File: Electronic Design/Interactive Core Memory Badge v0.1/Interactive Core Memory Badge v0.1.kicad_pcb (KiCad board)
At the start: 2 copper layers, 8 parts, among them Q1 MMBT4403LT1G, Q2 MMBT4401LT1G, U1 Teensy-LC

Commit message: Schematic Complete
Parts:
- removed the D1 at (103.5, 89.5)
- removed the D2 at (97.8, 86.4)
- removed the Q1 at (109.2, 95.2)
- removed the Q2 at (97.8, 95.2)
- removed the R1 at (104.5, 94.0)
- removed the R2 at (93.0, 94.0)
- added D1: BAW56S, Package_TO_SOT_SMD:SOT-363_SC-70-6, F.Cu at (99.1, 111.8)
- added D1: BAW56S, Package_TO_SOT_SMD:SOT-363_SC-70-6, F.Cu at (76.2, 111.8)
- added D2: BAV70S, Package_TO_SOT_SMD:SOT-363_SC-70-6, F.Cu at (99.1, 115.6)
- added D2: BAV70S, Package_TO_SOT_SMD:SOT-363_SC-70-6, F.Cu at (76.2, 115.6)
- added D3: BAW56S, Package_TO_SOT_SMD:SOT-363_SC-70-6, F.Cu at (110.2, 132.6)
- added D4: BAV70S, Package_TO_SOT_SMD:SOT-363_SC-70-6, F.Cu at (101.4, 140.5)
- added D5: BAW56S, Package_TO_SOT_SMD:SOT-363_SC-70-6, F.Cu at (63.0, 150.0)
- added D6: BAV70S, Package_TO_SOT_SMD:SOT-363_SC-70-6, F.Cu at (67.7, 147.0)
- added F1: Polyfuse, Fuse:Fuse_0805_2012Metric, F.Cu at (57.6, 160.7)
- added Q1: MMBT4403LT1G, Digikey:SOT-23-3, F.Cu at (89.9, 112.3)
- added Q1: MMBT4403LT1G, Digikey:SOT-23-3, F.Cu at (67.0, 112.3)
- added Q10: MMBT4401LT1G, Digikey:SOT-23-3, F.Cu at (45.0, 146.6)
- added Q11: MMBT4403LT1G, Digikey:SOT-23-3, F.Cu at (49.7, 141.7)
- added Q12: MMBT4401LT1G, Digikey:SOT-23-3, F.Cu at (45.0, 151.6)
- added Q13: MMBT4403LT1G, Digikey:SOT-23-3, F.Cu at (92.5, 135.2)
- added Q14: MMBT4401LT1G, Digikey:SOT-23-3, F.Cu at (87.8, 140.1)
- added Q15: MMBT4403LT1G, Digikey:SOT-23-3, F.Cu at (97.2, 130.2)
- added Q16: MMBT4401LT1G, Digikey:SOT-23-3, F.Cu at (92.5, 140.1)
- added Q17: MMBT4403LT1G, Digikey:SOT-23-3, F.Cu at (54.4, 141.7)
- added Q18: MMBT4401LT1G, Digikey:SOT-23-3, F.Cu at (49.7, 146.6)
- added Q19: MMBT4403LT1G, Digikey:SOT-23-3, F.Cu at (54.4, 146.6)
- added Q2: MMBT4401LT1G, Digikey:SOT-23-3, F.Cu at (94.6, 112.3)
- added Q2: MMBT4401LT1G, Digikey:SOT-23-3, F.Cu at (71.7, 112.3)
- added Q20: MMBT4401LT1G, Digikey:SOT-23-3, F.Cu at (49.7, 151.6)
- added Q21: MMBT4401LT1G, Digikey:SOT-23-3, F.Cu at (63.5, 188.0)
- added Q3: MMBT4403LT1G, Digikey:SOT-23-3, F.Cu at (83.1, 130.2)
- added Q4: MMBT4401LT1G, Digikey:SOT-23-3, F.Cu at (83.1, 135.2)
- added Q5: MMBT4403LT1G, Digikey:SOT-23-3, F.Cu at (87.8, 130.2)
- added Q6: MMBT4401LT1G, Digikey:SOT-23-3, F.Cu at (83.1, 140.1)
- added Q7: MMBT4403LT1G, Digikey:SOT-23-3, F.Cu at (92.5, 130.2)
- added Q8: MMBT4401LT1G, Digikey:SOT-23-3, F.Cu at (87.8, 135.2)
- added Q9: MMBT4403LT1G, Digikey:SOT-23-3, F.Cu at (45.0, 141.7)
- added R1: 220, Resistor_SMD:R_0805_2012Metric, F.Cu at (89.7, 116.3)
- added R1: 220, Resistor_SMD:R_0805_2012Metric, F.Cu at (66.9, 116.3)
- added R10: 6R8, Resistor_SMD:R_0805_2012Metric, F.Cu at (101.5, 134.2)
- added R11: 6R8, Resistor_SMD:R_0805_2012Metric, F.Cu at (59.0, 140.7)
- added R12: 6R8, Resistor_SMD:R_0805_2012Metric, F.Cu at (54.3, 150.6)
- added R13: 220, Resistor_SMD:R_0805_2012Metric, F.Cu at (101.5, 137.1)
- added R14: 220, Resistor_SMD:R_0805_2012Metric, F.Cu at (97.1, 140.1)
- added R15: 6R8, Resistor_SMD:R_0805_2012Metric, F.Cu at (105.9, 132.2)
- added R16: 220, Resistor_SMD:R_0805_2012Metric, F.Cu at (63.4, 140.7)
- added R17: 220, Resistor_SMD:R_0805_2012Metric, F.Cu at (59.0, 143.6)
- added R18: 220, Resistor_SMD:R_0805_2012Metric, F.Cu at (63.4, 143.6)
- added R19: 220, Resistor_SMD:R_0805_2012Metric, F.Cu at (59.0, 146.6)
- added R2: 220, Resistor_SMD:R_0805_2012Metric, F.Cu at (94.2, 116.3)
- added R2: 220, Resistor_SMD:R_0805_2012Metric, F.Cu at (71.3, 116.3)
- added R20: 220, Resistor_SMD:R_0805_2012Metric, F.Cu at (110.6, 129.2)
- added R21: 220, Resistor_SMD:R_0805_2012Metric, F.Cu at (105.9, 135.1)
- added R22: 6R8, Resistor_SMD:R_0805_2012Metric, F.Cu at (96.2, 144.1)
- added R23: 220, Resistor_SMD:R_0805_2012Metric, F.Cu at (58.7, 150.6)
- added R24: 220, Resistor_SMD:R_0805_2012Metric, F.Cu at (67.8, 140.7)
- added R25: 220, Resistor_SMD:R_0805_2012Metric, F.Cu at (63.4, 146.6)
- added R26: 220, Resistor_SMD:R_0805_2012Metric, F.Cu at (67.8, 143.6)
- added R27: 220, Resistor_SMD:R_0805_2012Metric, F.Cu at (68.1, 187.0)
- added R28: 1K5, Resistor_SMD:R_0805_2012Metric, F.Cu at (48.6, 82.5)
- added R29: 1K8, Resistor_SMD:R_0805_2012Metric, F.Cu at (67.7, 129.9)
- added R3: 220, Resistor_SMD:R_0805_2012Metric, F.Cu at (87.4, 144.1)
- added R30: 22, Resistor_SMD:R_0805_2012Metric, F.Cu at (67.7, 132.8)
- added R31: 1K5, Resistor_SMD:R_0805_2012Metric, F.Cu at (72.1, 129.9)
- added R32: 1K8, Resistor_SMD:R_0805_2012Metric, F.Cu at (67.7, 135.8)
- added R33: 22, Resistor_SMD:R_0805_2012Metric, F.Cu at (72.1, 132.8)
- added R34: 1K5, Resistor_SMD:R_0805_2012Metric, F.Cu at (76.5, 129.9)
- added R35: 10k, Resistor_SMD:R_0805_2012Metric, F.Cu at (72.1, 135.8)
- added R36: 10k, Resistor_SMD:R_0805_2012Metric, F.Cu at (62.7, 165.1)
- added R37: 10k, Resistor_SMD:R_0805_2012Metric, F.Cu at (62.6, 171.0)
- added R38: 4K7, Resistor_SMD:R_0805_2012Metric, F.Cu at (67.0, 171.3)
- added R39: 4K7, Resistor_SMD:R_0805_2012Metric, F.Cu at (67.0, 175.7)
- added R4: 220, Resistor_SMD:R_0805_2012Metric, F.Cu at (91.8, 144.1)
- added R5: 6R8, Resistor_SMD:R_0805_2012Metric, F.Cu at (83.0, 144.1)
- added R6: 220, Resistor_SMD:R_0805_2012Metric, F.Cu at (101.8, 129.2)
- added R7: 220, Resistor_SMD:R_0805_2012Metric, F.Cu at (97.1, 134.2)
- added R8: 220, Resistor_SMD:R_0805_2012Metric, F.Cu at (97.1, 137.1)
- added R9: 220, Resistor_SMD:R_0805_2012Metric, F.Cu at (106.2, 129.2)
- added SW1: SW_SPST, Digikey:Switch_Slide_JS202011SCQN, F.Cu at (48.3, 162.8)
- added U1: Micro_LiPo_Charger, Core_Memory_8x8_Array:Micro_LiPo_Charger, F.Cu at (54.6, 182.9)
- added U3: LM393, Digikey:SOIC-8_W3.9mm, F.Cu at (46.4, 91.3)
- moved CM1 43.3 mm to (83.8, 76.2)
- moved U2 41.5 mm to (83.8, 175.3)
- renumbered U1 to U2
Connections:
- net Net-(U1-Pad19) renamed AVAILABLE
- net Net-(U1-Pad37) renamed REED_SWITCH
- CM1 pad 1: XT0 -> XT0-4
- CM1 pad 10: Net-(CM1-Pad10) -> YL1
- CM1 pad 11: Net-(CM1-Pad11) -> YL2
- CM1 pad 12: Net-(CM1-Pad12) -> YL3
- CM1 pad 13: Net-(CM1-Pad13) -> YL4
- CM1 pad 14: Net-(CM1-Pad10) -> YL5
- CM1 pad 15: Net-(CM1-Pad11) -> YL4
- CM1 pad 16: Net-(CM1-Pad12) -> YL5
- CM1 pad 2: XT1 -> XT1-5
- CM1 pad 29: Net-(CM1-Pad29) -> Net-(CM1-Pad25)
- CM1 pad 3: XT2 -> XT2-6
- CM1 pad 30: Net-(CM1-Pad30) -> Net-(CM1-Pad26)
- CM1 pad 31: Net-(CM1-Pad31) -> Net-(CM1-Pad27)
- CM1 pad 32: Net-(CM1-Pad32) -> Net-(CM1-Pad28)
- CM1 pad 4: XT3 -> XT3-7
- CM1 pad 5: XT4 -> XT0-4
- CM1 pad 6: XT5 -> XT1-5
- CM1 pad 7: XT6 -> XT2-6
- CM1 pad 8: XT7 -> XT3-7
- CM1 pad 9: Net-(CM1-Pad13) -> YL0
- U2 pad 1: Net-(U1-Pad1) -> -BATT
- U2 pad 10: Net-(U1-Pad10) -> Q4N
- U2 pad 11: Net-(U1-Pad11) -> Q5P
- U2 pad 12: Net-(U1-Pad12) -> Q5N
- U2 pad 13: Net-(U1-Pad13) -> Q6P
- U2 pad 14: Net-(U1-Pad14) -> Q6N
- U2 pad 2: Net-(U1-Pad2) -> SENSE_PULSE
- U2 pad 20: Net-(U1-Pad20) -> Q7P
- U2 pad 21: Net-(U1-Pad21) -> Q7N
- U2 pad 22: Net-(U1-Pad22) -> Q8P
- U2 pad 23: Net-(U1-Pad23) -> Q8N
- U2 pad 24: Net-(U1-Pad24) -> Q9P
- U2 pad 25: Net-(U1-Pad25) -> I2C_DATA
- U2 pad 26: Net-(U1-Pad26) -> I2C_CLOCK
- U2 pad 27: Net-(U1-Pad27) -> Q9N
- U2 pad 28: Net-(U1-Pad28) -> Q10P
- U2 pad 29: Net-(U1-Pad29) -> Q10N
- U2 pad 30: Net-(U1-Pad30) -> WRITE_ENABLE
- U2 pad 31: Net-(U1-Pad31) -> +3V3
- U2 pad 32: Net-(U1-Pad32) -> -BATT
- U2 pad 33: +BATT -> +VSW
- U2 pad 34: Net-(U1-Pad34) -> V+USB
- U2 pad 35: Net-(U1-Pad35) -> +3V3
- U2 pad 5: Net-(U1-Pad5) -> Q2P
- U2 pad 6: Net-(U1-Pad6) -> Q2N
- U2 pad 7: Net-(U1-Pad7) -> Q3P
- U2 pad 8: Net-(U1-Pad8) -> Q3N
- U2 pad 9: Net-(U1-Pad9) -> Q4P
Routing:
- net Q1N: track 61.8 -> 0.00 mm
- net Q1P: track 57.9 -> 0.00 mm, vias 2 -> 0
- net -BATT: track 47.5 -> 0.00 mm
- net Net-(CM1-Pad26): track 0.00 -> 27.7 mm
- net Net-(CM1-Pad25): track 0.00 -> 27.7 mm
- net XT3-7: track 0.00 -> 27.6 mm
- net XT1-5: track 0.00 -> 27.6 mm
- net XT2-6: track 0.00 -> 27.4 mm
- net XT0-4: track 0.00 -> 27.4 mm
- net Net-(CM1-Pad28): track 0.00 -> 27.4 mm
- net Net-(CM1-Pad27): track 0.00 -> 24.3 mm
- net XB4: track 16.2 -> 0.00 mm, vias 2 -> 0
- net Net-(D1-Pad3): track 14.7 -> 0.00 mm
- net Net-(D2-Pad3): track 11.8 -> 0.00 mm
- net XB5: track 11.2 -> 0.00 mm, vias 2 -> 0
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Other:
- board outline added: 81.3 x 165.1 mm

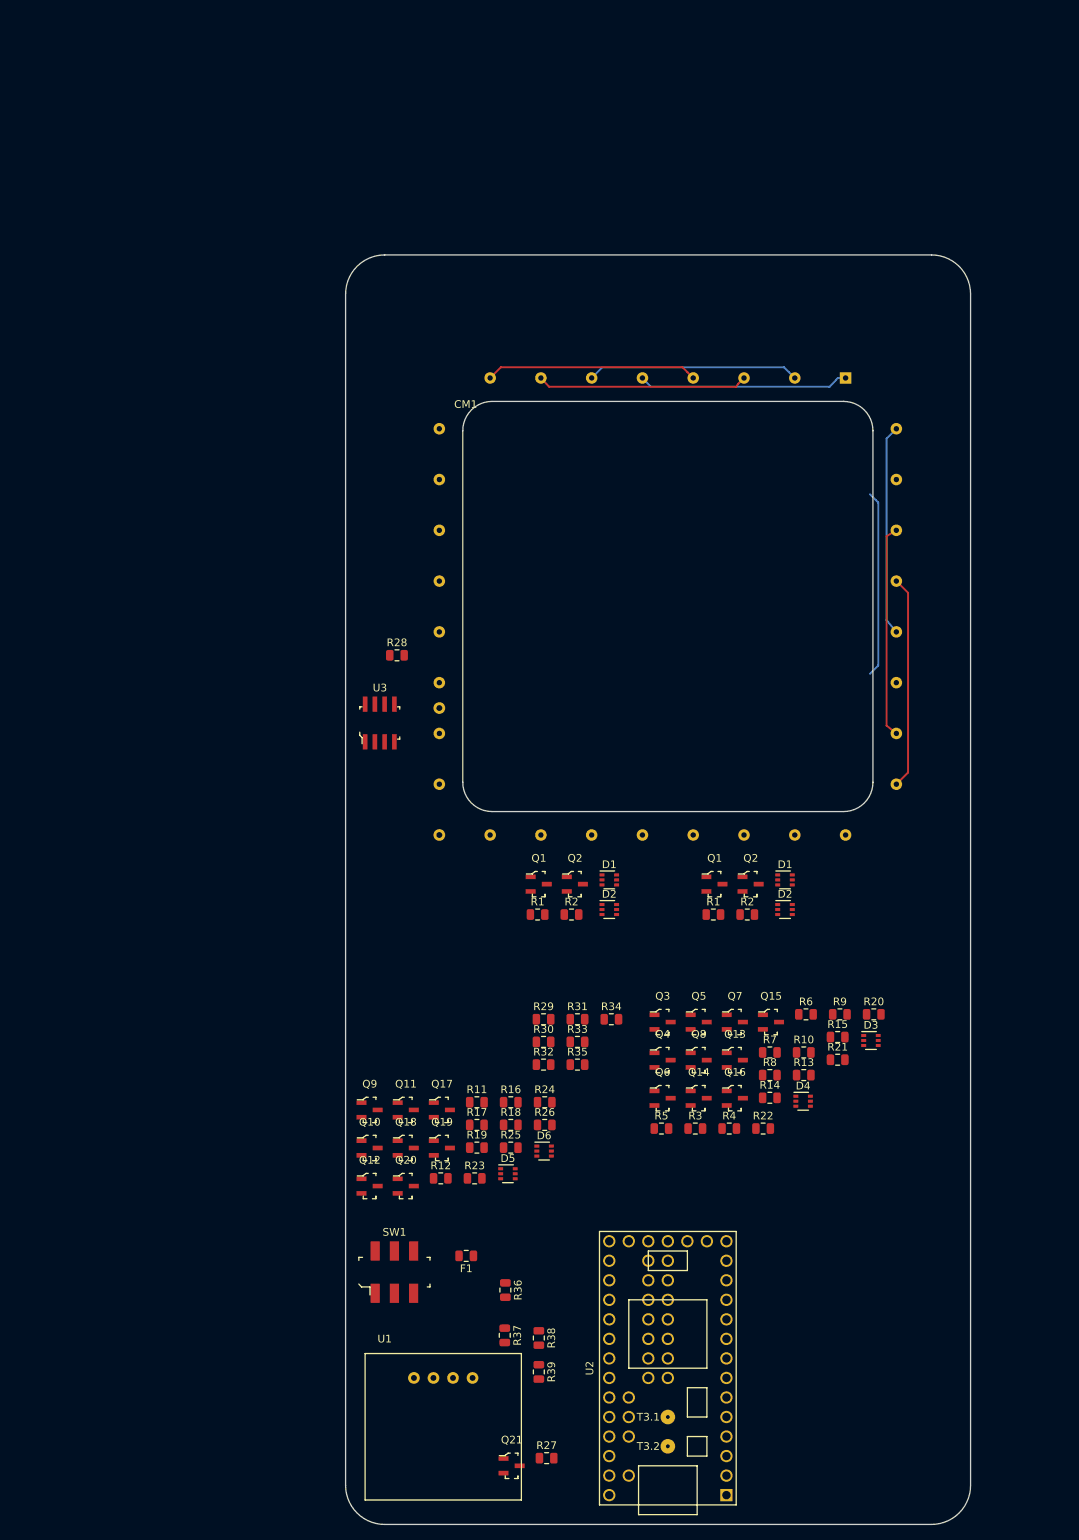
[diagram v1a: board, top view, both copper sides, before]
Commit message: Layout 75% complete for V0.1
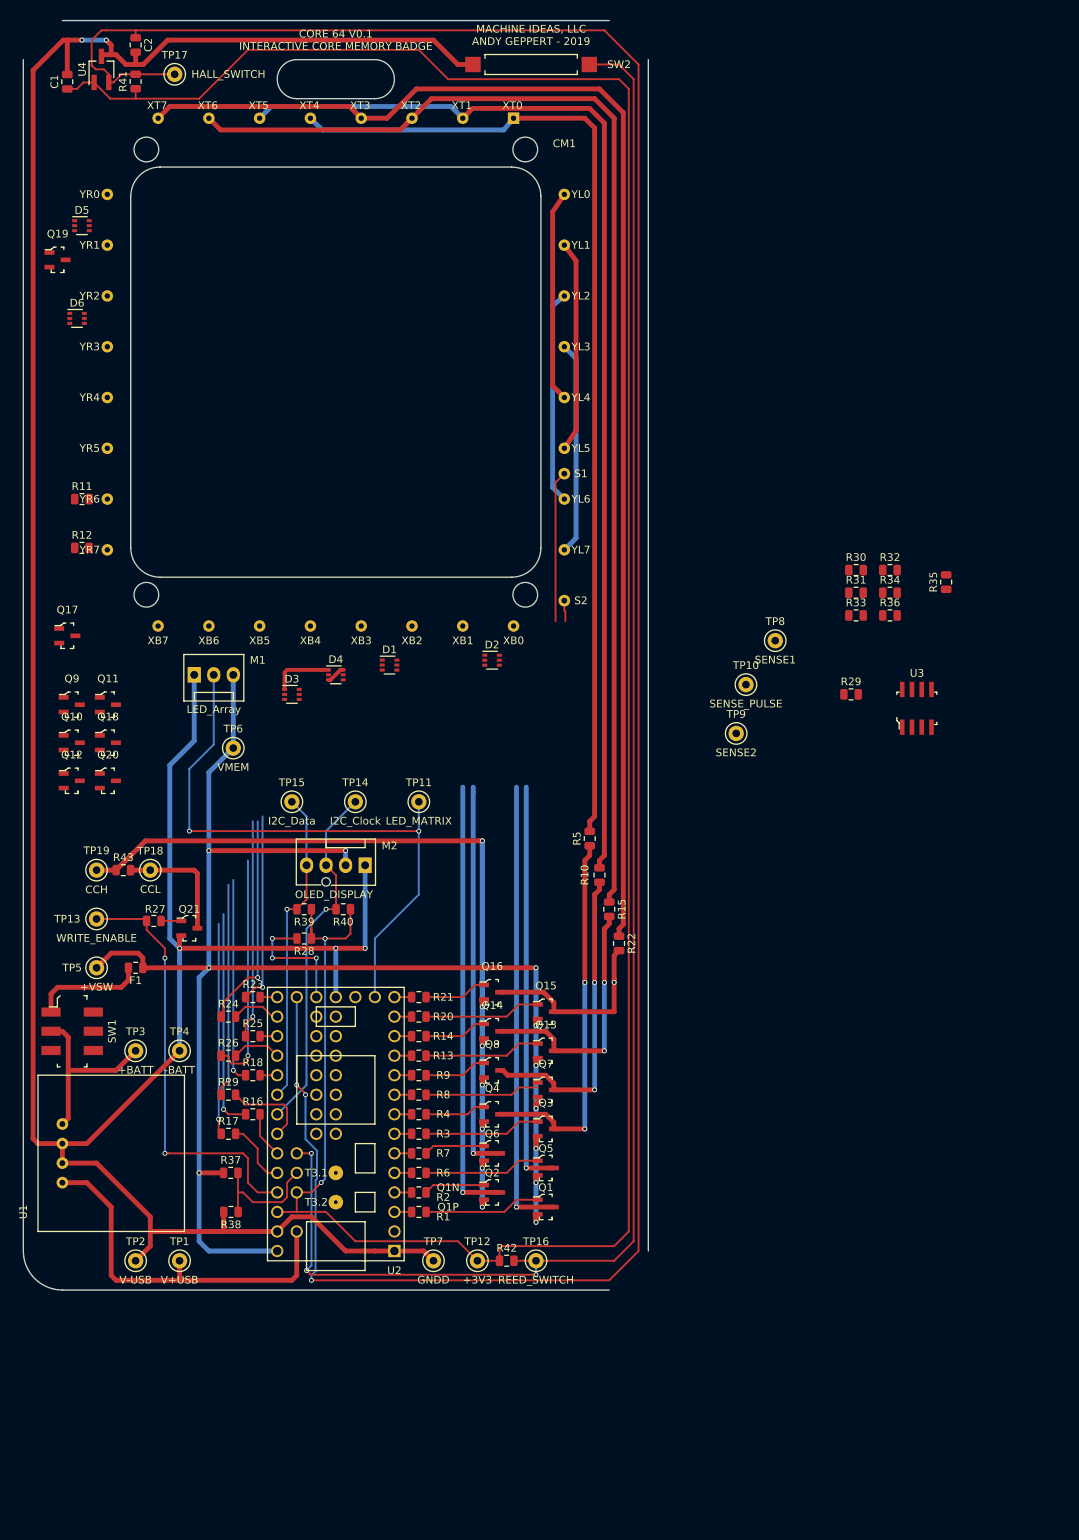
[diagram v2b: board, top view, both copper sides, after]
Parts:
- removed the D1 at (99.1, 111.8)
- removed the D1 at (76.2, 111.8)
- removed the D2 at (99.1, 115.6)
- removed the D2 at (76.2, 115.6)
- removed the Q1 at (89.9, 112.3)
- removed the Q1 at (67.0, 112.3)
- removed the Q2 at (94.6, 112.3)
- removed the Q2 at (71.7, 112.3)
- removed the R1 at (89.7, 116.3)
- removed the R1 at (66.9, 116.3)
- removed the R2 at (94.2, 116.3)
- removed the R2 at (71.3, 116.3)
- removed the R38 at (67.0, 171.3)
- added C1: 0.1uF, Capacitor_SMD:C_0805_2012Metric, F.Cu at (5.71, 7.95)
- added C2: 10pF, Capacitor_SMD:C_0805_2012Metric, F.Cu at (14.6, 3.17)
- added D1: BAW56S, Package_TO_SOT_SMD:SOT-363_SC-70-6, F.Cu at (47.6, 83.8)
- added D2: BAV70S, Package_TO_SOT_SMD:SOT-363_SC-70-6, F.Cu at (61.0, 83.2)
- added M1: LED_Array, Core_Memory_8x8_Array:LED_Matrix_Header_3pin, F.Cu at (22.2, 85.1)
- added M2: OLED_DISPLAY, Core_Memory_8x8_Array:OLED_Header_4PIN, F.Cu at (44.5, 109.9)
- added Q1: MMBT4403LT1G, Digikey:SOT-23-3, F.Cu at (67.9, 154.3)
- added Q2: MMBT4401LT1G, Digikey:SOT-23-3, F.Cu at (61.0, 152.4)
- added R1: 220, Resistor_SMD:R_0805_2012Metric, F.Cu at (51.4, 154.9)
- added R2: 220, Resistor_SMD:R_0805_2012Metric, F.Cu at (51.4, 152.4)
- added R29: 1K5, Resistor_SMD:R_0805_2012Metric, F.Cu at (107.6, 87.6)
- added R40: 4K7, Resistor_SMD:R_0805_2012Metric, F.Cu at (41.6, 115.6)
- added R41: 4K7, Resistor_SMD:R_0805_2012Metric, F.Cu at (14.6, 7.92)
- added R42: 4K7, Resistor_SMD:R_0805_2012Metric, F.Cu at (62.9, 161.3)
- added R43: 0, Resistor_SMD:R_0805_2012Metric, F.Cu at (13.0, 110.5)
- added SW2: SW_Reed, Button_Switch_SMD:SW_SPST_REED_CT10-XXXX-G1, F.Cu at (66.0, 5.71)
- added TP1: V+USB, TestPoint:TestPoint_Keystone_5000-5004_Miniature, F.Cu at (20.3, 161.3)
- added TP10: SENSE_PULSE, TestPoint:TestPoint_Keystone_5000-5004_Miniature, F.Cu at (94.0, 86.4)
- added TP11: LED_MATRIX, TestPoint:TestPoint_Keystone_5000-5004_Miniature, F.Cu at (51.4, 101.6)
- added TP12: +3V3, TestPoint:TestPoint_Keystone_5000-5004_Miniature, F.Cu at (59.1, 161.3)
- added TP13: WRITE_ENABLE, TestPoint:TestPoint_Keystone_5000-5004_Miniature, F.Cu at (9.53, 116.8)
- added TP14: I2C_Clock, TestPoint:TestPoint_Keystone_5000-5004_Miniature, F.Cu at (43.2, 101.6)
- added TP15: I2C_Data, TestPoint:TestPoint_Keystone_5000-5004_Miniature, F.Cu at (34.9, 101.6)
- added TP16: REED_SWITCH, TestPoint:TestPoint_Keystone_5000-5004_Miniature, F.Cu at (66.7, 161.3)
- added TP17: HALL_SWITCH, TestPoint:TestPoint_Keystone_5000-5004_Miniature, F.Cu at (19.7, 6.99)
- added TP18: CCL, TestPoint:TestPoint_Keystone_5000-5004_Miniature, F.Cu at (16.5, 110.5)
- added TP19: CCH, TestPoint:TestPoint_Keystone_5000-5004_Miniature, F.Cu at (9.53, 110.5)
- added TP2: V-USB, TestPoint:TestPoint_Keystone_5000-5004_Miniature, F.Cu at (14.6, 161.3)
- added TP3: +BATT, TestPoint:TestPoint_Keystone_5000-5004_Miniature, F.Cu at (14.6, 134.0)
- added TP4: -BATT, TestPoint:TestPoint_Keystone_5000-5004_Miniature, F.Cu at (20.3, 134.0)
- added TP5: +VSW, TestPoint:TestPoint_Keystone_5000-5004_Miniature, F.Cu at (9.53, 123.2)
- added TP6: VMEM, TestPoint:TestPoint_Keystone_5000-5004_Miniature, F.Cu at (27.3, 94.6)
- added TP7: GNDD, TestPoint:TestPoint_Keystone_5000-5004_Miniature, F.Cu at (53.3, 161.3)
- added TP8: SENSE1, TestPoint:TestPoint_Keystone_5000-5004_Miniature, F.Cu at (97.8, 80.6)
- added TP9: SENSE2, TestPoint:TestPoint_Keystone_5000-5004_Miniature, F.Cu at (92.7, 92.7)
- added U4: A3214ELHLT-T, Package_TO_SOT_SMD:SOT-23W_Handsoldering, F.Cu at (10.2, 6.35)
- R28: value 1K5 -> 4K7
- moved D5 135.2 mm to (7.62, 26.7)
- moved Q19 125.9 mm to (4.45, 31.1)
- moved D6 124.2 mm to (6.99, 38.7)
- moved R12 94.3 mm to (7.62, 68.6)
- moved R11 93.8 mm to (7.62, 62.2)
- moved D3 87.7 mm to (34.9, 87.6)
- moved R27 86.6 mm to (17.0, 117.1), turned to 180 degrees
- moved D4 82.3 mm to (40.6, 85.1)
- moved Q21 81.5 mm to (21.6, 118.0)
- moved Q17 78.6 mm to (5.71, 80.0)
- moved R35 71.6 mm to (120.0, 73.0), turned to 90 degrees
- moved R31 71.2 mm to (108.3, 74.4)
- moved R33 71.2 mm to (108.3, 77.4)
- moved R34 71.2 mm to (112.7, 74.4)
- moved R36 71.2 mm to (112.7, 77.4)
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- renumbered R29 to R30, R30 to R31, R31 to R32, R32 to R33, R33 to R34, R34 to R35, R35 to R36, R36 to R37, R37 to R38
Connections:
- Q21 pad 3: GNDPWR -> Net-(Q21-Pad3)
- R28 pad 1: SENSE1 -> +3V3
- R28 pad 2: SENSE2 -> Net-(R28-Pad2)
- R39 pad 2: I2C_CLOCK -> I2C_DATA
- SW1 pad 1: +BATT -> Net-(F1-Pad2)
- SW1 pad 2: Net-(F1-Pad2) -> +BATT
- U2 pad 15: Net-(U2-Pad15) -> LED_MATRIX
- U2 pad 18: Net-(U2-Pad18) -> Net-(R28-Pad2)
- U2 pad 19: AVAILABLE -> HALL_SWITCH
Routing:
- net -BATT: track 0.00 -> 396.3 mm, vias 0 -> 5
- net +3V3: track 0.00 -> 332.2 mm, vias 0 -> 2
- net HALL_SWITCH: track 0.00 -> 327.4 mm, vias 0 -> 3
- net REED_SWITCH: track 0.00 -> 223.6 mm, vias 0 -> 3
- net +VSW: track 0.00 -> 208.4 mm, vias 0 -> 11
- net GNDPWR: track 0.00 -> 153.3 mm, vias 0 -> 7
- net XT3-7: track 27.6 -> 171.9 mm
- net XT2-6: track 27.4 -> 158.3 mm
- net XT1-5: track 27.6 -> 144.5 mm
- net XT0-4: track 27.4 -> 130.6 mm
- net LED_MATRIX: track 0.00 -> 79.2 mm, vias 0 -> 2
- net Net-(D1-Pad3): track 0.00 -> 59.5 mm, vias 0 -> 1
- net Net-(D2-Pad3): track 0.00 -> 57.6 mm, vias 0 -> 1
- net WRITE_ENABLE: track 0.00 -> 56.4 mm, vias 0 -> 2
- net Net-(D4-Pad3): track 0.00 -> 53.6 mm, vias 0 -> 1
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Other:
- outline, holes or cut-outs redrawn
- net class Core Current added: clearance 0.127, trace_width 0.635, via_dia 0.635, via_drill 0.4
- net class Core Current 20mil added: clearance 0.127, trace_width 0.508, via_dia 0.635, via_drill 0.4
- net class Default: clearance 0.2 -> 0.127; trace_width 0.25 -> 0.254; via_dia 0.8 -> 0.635
- rule trace_clearance: 0.2 -> 0.127
- board text added: "CORE 64 V0.1 INTERACTIVE CORE MEMORY BADGE"
- board text added: "MACHINE IDEAS, LLC ANDY GEPPERT - 2019"
- board text added: "Q1N"
- board text added: "Q1P"
